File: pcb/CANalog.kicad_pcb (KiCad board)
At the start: 2 copper layers, 97 parts, among them J1 PWR, J2 USB_B_Micro, J3 SPI3, J4 I2C2, J5 STM_PROG, J6 ESP_PROG, J7 AOUT, J8 CAN, Q1 DMP3099L-7, Q2 MMBT2222A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

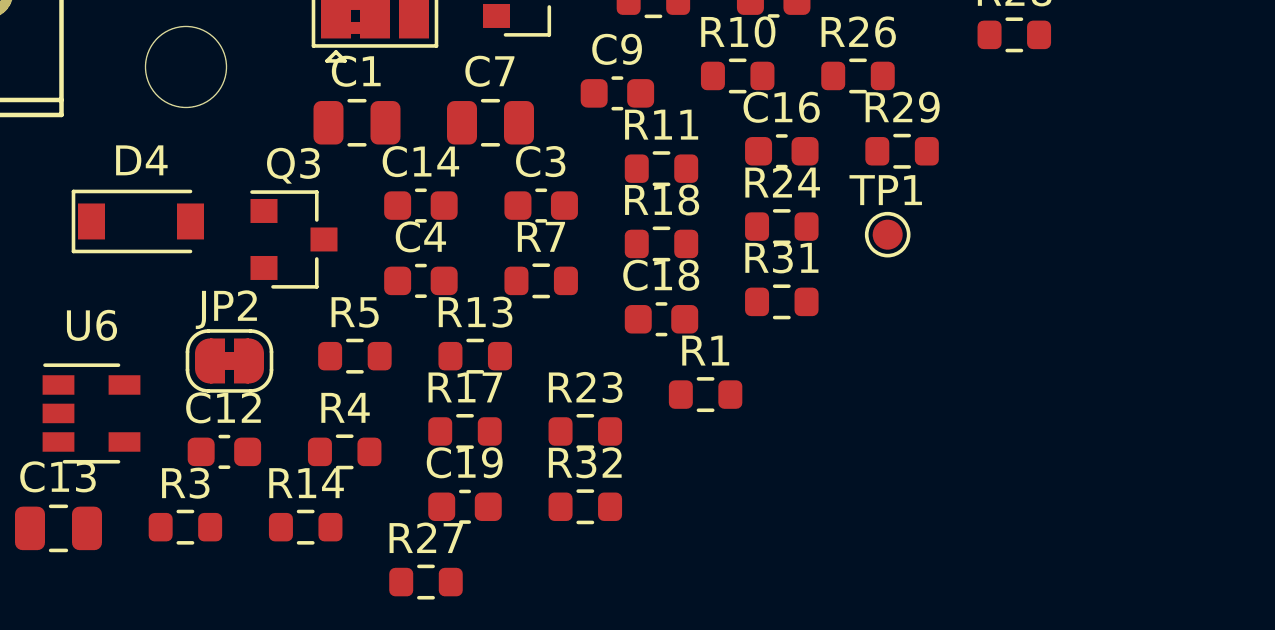
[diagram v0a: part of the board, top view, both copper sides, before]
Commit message: replace agnd jumper to gnd with net tie
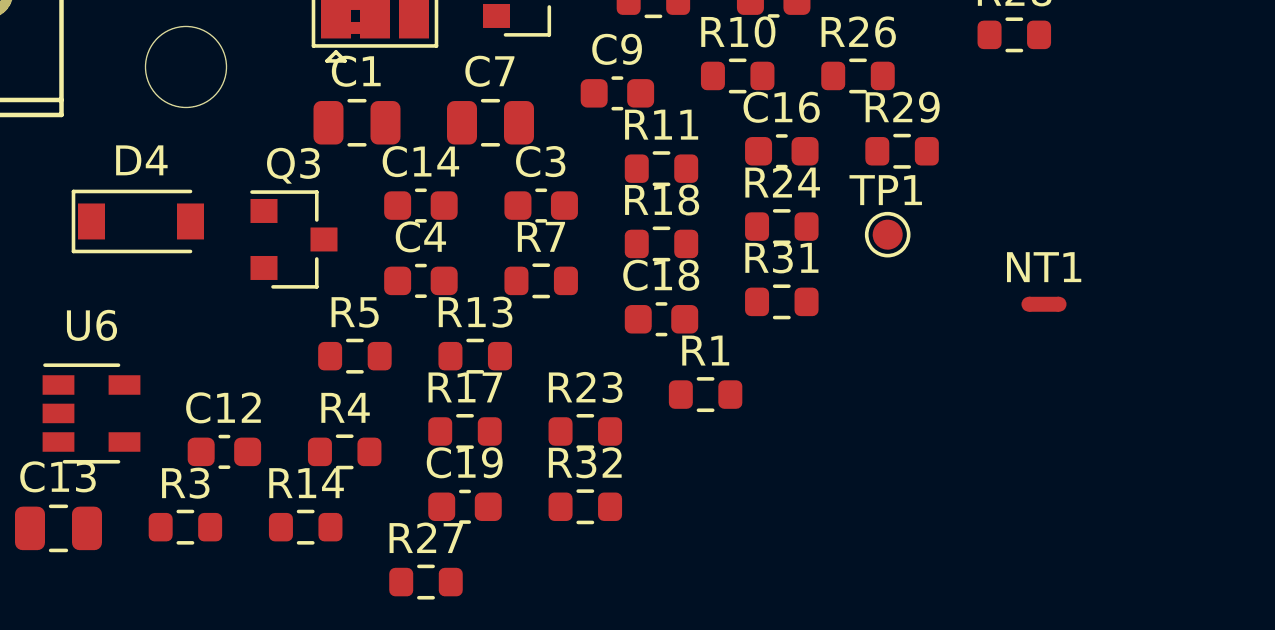
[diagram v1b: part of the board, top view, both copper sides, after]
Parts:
- removed JP2: NC, Jumper:SolderJumper-2_P1.3mm_Bridged_RoundedPad1.0x1.5mm
- added NT1: Net-Tie_2, NetTie:NetTie-2_SMD_Pad0.5mm, F.Cu at (173.0, 106.0)
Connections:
- J2 pad 4: (no net) -> Net-(J2-Pad4)
- J5 pad 1: (no net) -> Net-(J5-Pad1)
- J6 pad 1: (no net) -> Net-(J6-Pad1)
- J6 pad 4: (no net) -> Net-(J6-Pad4)
- J6 pad 5: (no net) -> Net-(J6-Pad5)
- U3 pad 15: (no net) -> Net-(U3-Pad15)
- U3 pad 16: (no net) -> Net-(U3-Pad16)
- U3 pad 17: (no net) -> Net-(U3-Pad17)
- U3 pad 2: (no net) -> Net-(U3-Pad2)
- U3 pad 21: (no net) -> Net-(U3-Pad21)
- U3 pad 29: (no net) -> Net-(U3-Pad29)
- U3 pad 3: (no net) -> Net-(U3-Pad3)
- U3 pad 4: (no net) -> Net-(U3-Pad4)
- U4 pad 17: (no net) -> Net-(U4-Pad17)
- U4 pad 18: (no net) -> Net-(U4-Pad18)
- U4 pad 19: (no net) -> Net-(U4-Pad19)
- U4 pad 2: (no net) -> Net-(U4-Pad2)
- U4 pad 20: (no net) -> Net-(U4-Pad20)
- U4 pad 21: (no net) -> Net-(U4-Pad21)
- U4 pad 22: (no net) -> Net-(U4-Pad22)
- U4 pad 4: (no net) -> Net-(U4-Pad4)
- U5 pad 4: (no net) -> Net-(U5-Pad4)
- U7 pad 5: (no net) -> Net-(U7-Pad5)

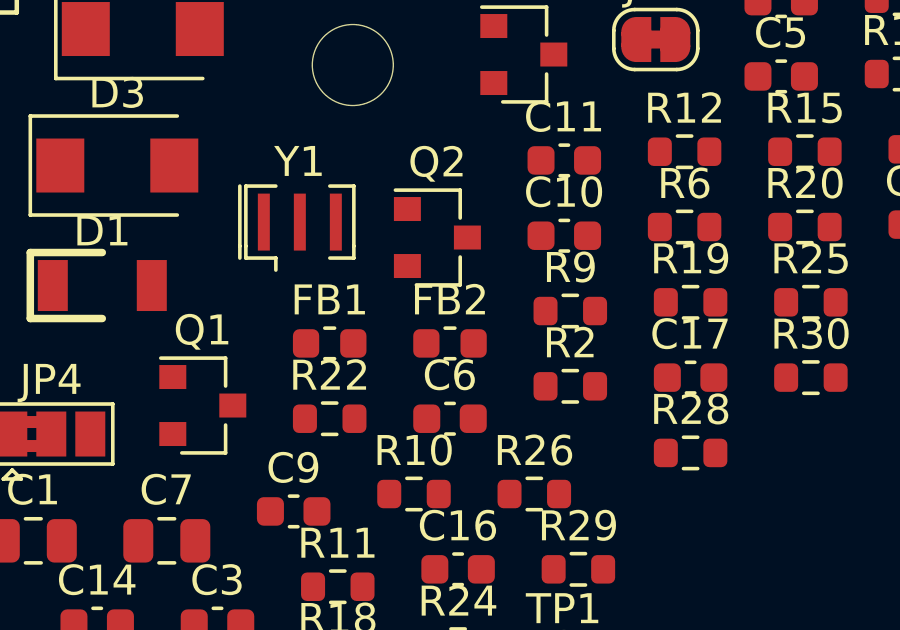
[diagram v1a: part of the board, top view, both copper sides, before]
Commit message: remove ferrite bead on analog output
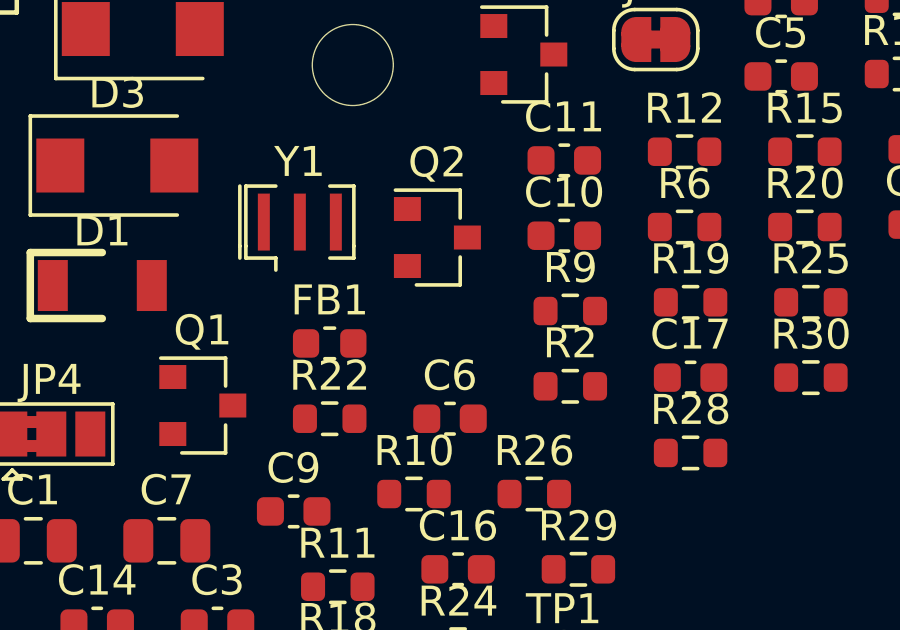
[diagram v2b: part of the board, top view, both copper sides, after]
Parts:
- removed FB2: FBS, Inductor_SMD:L_0603_1608Metric
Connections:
- J7 pad 1: Net-(FB2-Pad2) -> Net-(J7-Pad1)
- R26 pad 1: Net-(FB2-Pad1) -> Net-(J7-Pad1)
- U6 pad 1: Net-(FB2-Pad1) -> Net-(J7-Pad1)

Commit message: analog ground for analog circuit section
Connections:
- C17 pad 2: GND -> GNDA
- C18 pad 2: GND -> GNDA
- J7 pad 2: GND -> GNDA
- R25 pad 2: GND -> GNDA
- U6 pad 2: GND -> GNDA

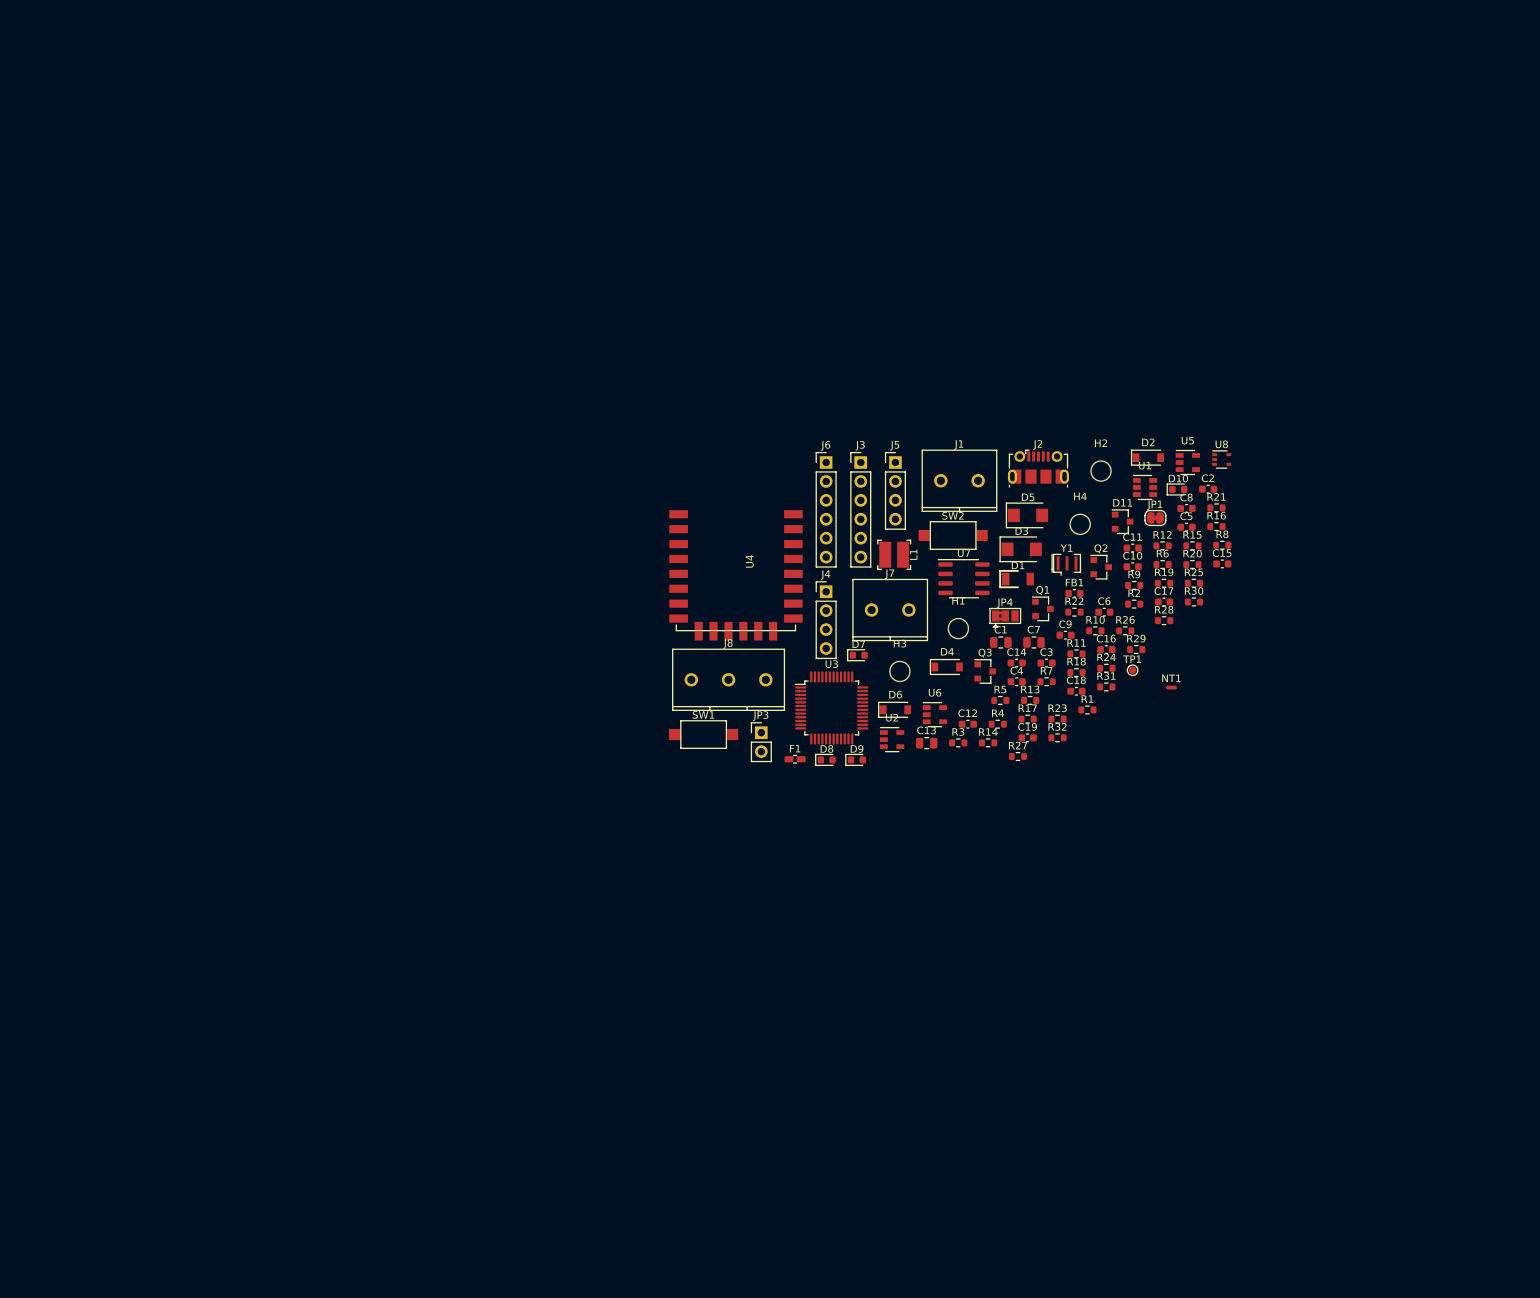
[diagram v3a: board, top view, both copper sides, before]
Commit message: start pcb layout
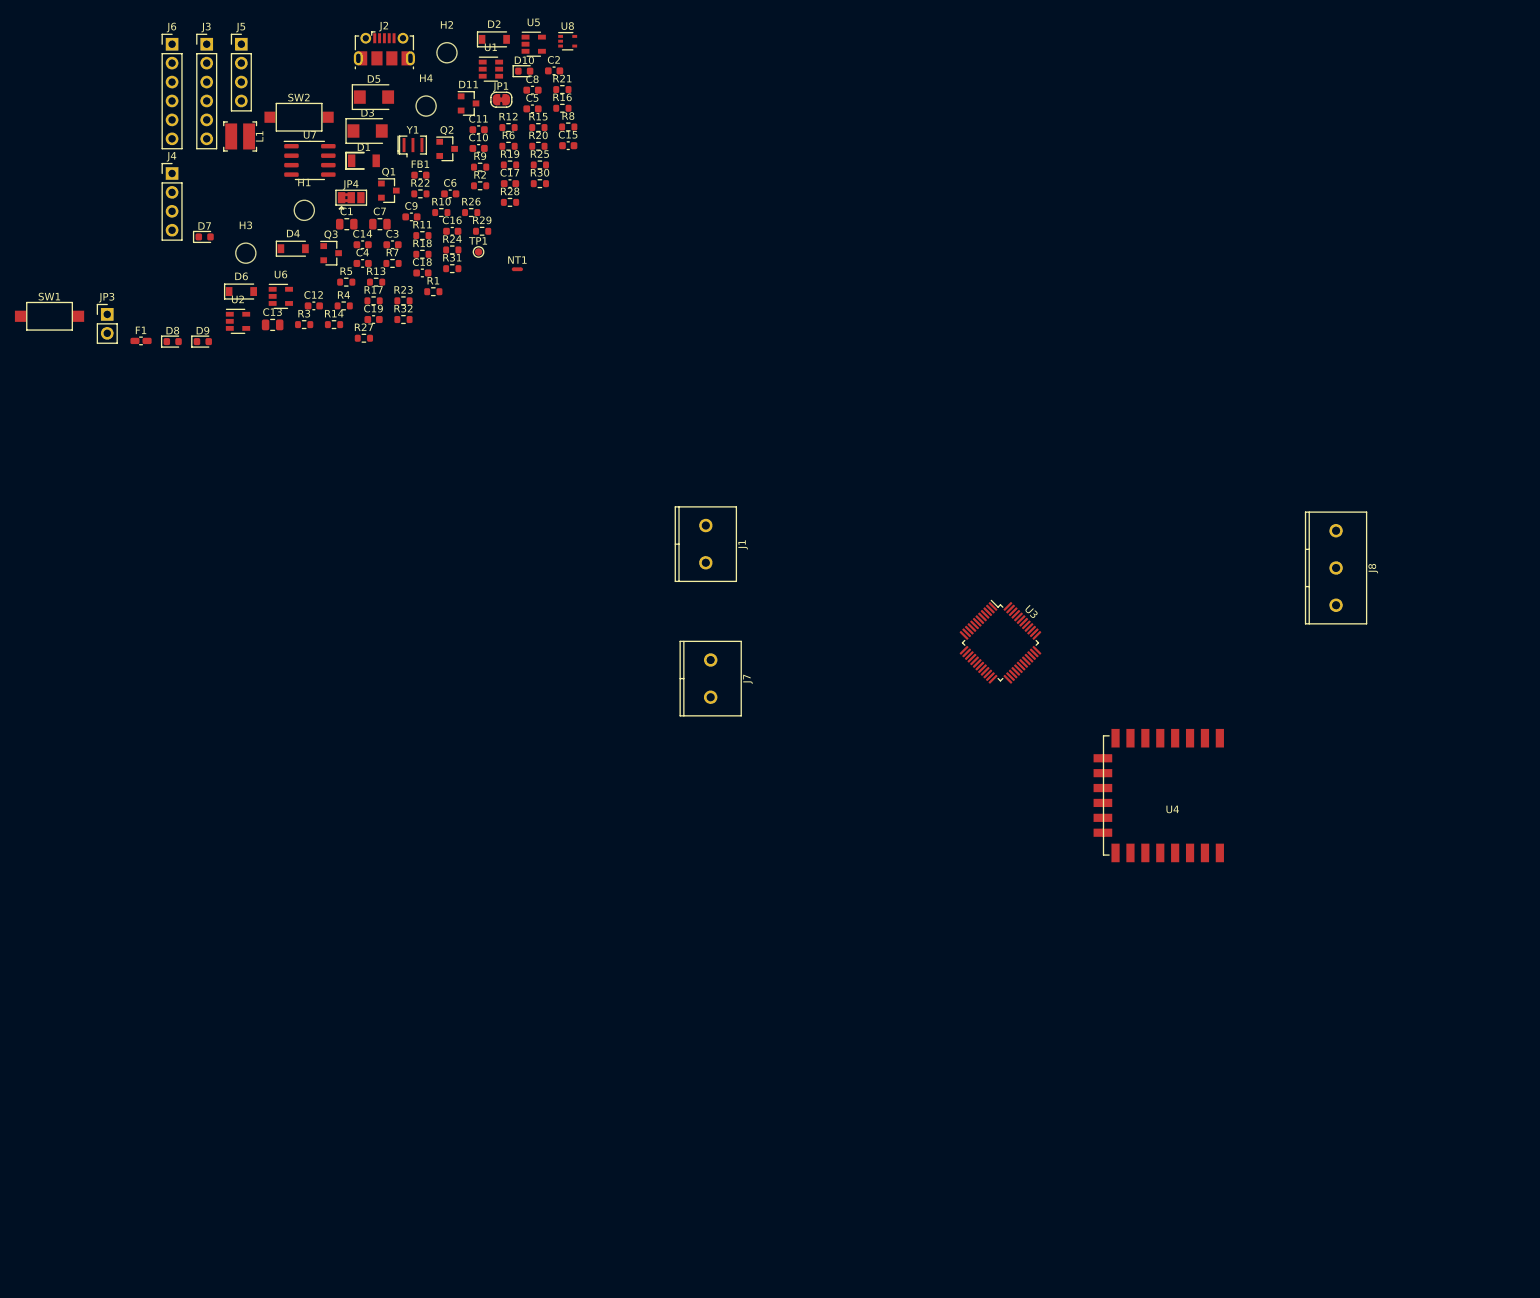
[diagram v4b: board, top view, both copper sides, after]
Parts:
- moved C1 104.2 mm to (62.3, 43.8)
- moved C16 104.2 mm to (76.5, 44.8)
- moved C17 104.2 mm to (84.2, 38.4)
- moved C18 104.2 mm to (72.5, 50.4)
- moved C5 104.2 mm to (87.2, 28.3)
- moved C9 104.2 mm to (71.0, 42.8)
- moved D5 104.2 mm to (66.0, 26.7)
- moved H4 104.2 mm to (73.0, 27.9)
- moved L1 104.2 mm to (48.0, 32.0)
- moved NT1 104.2 mm to (85.2, 49.9)
- moved Q1 104.2 mm to (68.0, 39.3)
- moved Q2 104.2 mm to (75.8, 33.7)
- moved Q3 104.2 mm to (60.2, 47.7)
- moved R1 104.2 mm to (73.9, 52.9)
- moved R10 104.2 mm to (75.0, 42.2)
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
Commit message: Update CANalog.kicad_pcb
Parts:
- moved U7 166.6 mm to (215.8, 86.5)
- moved H3 159.9 mm to (193.3, 116.2)
- moved JP4 159.2 mm to (217.3, 79.0)
- moved R27 153.8 mm to (214.7, 92.7)
- moved SW1 149.8 mm to (172.1, 60.0)
- moved U8 148.1 mm to (219.2, 95.1)
- moved C19 145.5 mm to (208.2, 87.0)
- moved R32 143.2 mm to (208.7, 91.8)
- moved C16 142.3 mm to (208.8, 97.0)
- moved D11 140.2 mm to (208.0, 81.7)
- moved D6 135.7 mm to (182.2, 73.7)
- moved H4 125.1 mm to (191.9, 66.5)
- moved R18 116.4 mm to (149.8, 134.8)
- moved R16 116.0 mm to (149.8, 128.3)
- moved R17 114.2 mm to (149.8, 131.6)
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
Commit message: Update CANalog.kicad_pcb
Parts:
- moved D9 123.8 mm to (173.1, 115.2)
- moved R29 123.8 mm to (164.4, 114.2)
- moved R31 123.8 mm to (164.7, 120.4)
- moved D7 123.8 mm to (171.1, 109.8)
- moved D8 123.8 mm to (169.0, 115.2)
- moved R28 123.8 mm to (164.2, 110.0)
- moved R30 123.8 mm to (164.5, 117.4)
- moved D10 123.8 mm to (170.8, 120.3)
- moved R12 43.6 mm to (59.4, 109.6)
- moved R8 38.4 mm to (67.2, 113.3)
- moved R9 34.9 mm to (67.3, 111.5)
- moved D3 30.5 mm to (65.3, 102.2), turned to 270 degrees
- moved D2 30.0 mm to (64.0, 112.8), turned to 90 degrees
- moved U1 28.3 mm to (65.8, 107.5)
- moved R7 28.1 mm to (69.7, 109.7), turned to 90 degrees
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
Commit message: Update CANalog.kicad_pcb
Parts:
- moved H1 108.9 mm to (28.0, 143.0)
- moved H2 105.5 mm to (28.0, 182.0)
- moved J1 105.4 mm to (30.0, 152.3)
- moved J7 104.6 mm to (30.0, 168.3)
- moved H4 103.7 mm to (122.0, 143.0)
- moved H3 97.1 mm to (122.0, 182.0)
- moved R3 55.4 mm to (54.6, 119.4), turned to 180 degrees
- moved Q1 50.7 mm to (53.2, 114.9), turned to 180 degrees
- moved D1 43.4 mm to (58.4, 115.6), turned to 270 degrees
- moved C9 25.6 mm to (76.4, 116.7), turned to 90 degrees
- moved D5 24.7 mm to (67.9, 121.4), turned to 180 degrees
- moved C7 20.7 mm to (73.2, 116.7), turned to 90 degrees
- moved L1 15.0 mm to (62.6, 115.9), turned to 270 degrees
- moved D3 14.2 mm to (66.8, 116.3), turned to 90 degrees
- moved C1 14.0 mm to (59.1, 110.0), turned to 90 degrees
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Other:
- board outline added: 100 x 45 mm

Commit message: Update CANalog.kicad_pcb
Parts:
- moved R24 108.7 mm to (41.0, 167.7)
- moved C17 106.2 mm to (36.8, 165.2)
- moved R26 105.7 mm to (41.0, 169.7)
- moved R25 105.1 mm to (41.0, 165.7), turned to 180 degrees
- moved C18 104.9 mm to (36.8, 167.2)
- moved U6 103.3 mm to (37.1, 170.3), turned to 90 degrees
- moved Q3 57.1 mm to (66.4, 127.2)
- moved U2 53.7 mm to (62.4, 127.4), turned to 90 degrees
- moved C11 52.8 mm to (59.2, 127.4), turned to 270 degrees
- moved C7 52.5 mm to (36.3, 154.1)
- moved R8 46.9 mm to (38.8, 144.0), turned to 270 degrees
- moved D5 46.8 mm to (38.8, 158.1)
- moved C1 46.1 mm to (36.3, 150.1), turned to 270 degrees
- moved D2 44.6 mm to (44.9, 143.7), turned to 0 degrees
- moved R12 44.5 mm to (49.6, 146.8), turned to 90 degrees
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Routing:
- added copper zone on B.Cu, net GND
